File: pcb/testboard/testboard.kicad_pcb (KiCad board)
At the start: 2 copper layers, 24 parts, among them IC1 TLE94112ESXUMA1, IC2 AP63203WU-7, J1 Left Socket, J2 Right Socket, J3 Motor 1, J4 Motor 2, J5 Motor 3, J6 USB_C_Receptacle_USB2.0_14P, SW1 Control, U1 CYPD3177-24LQXQ

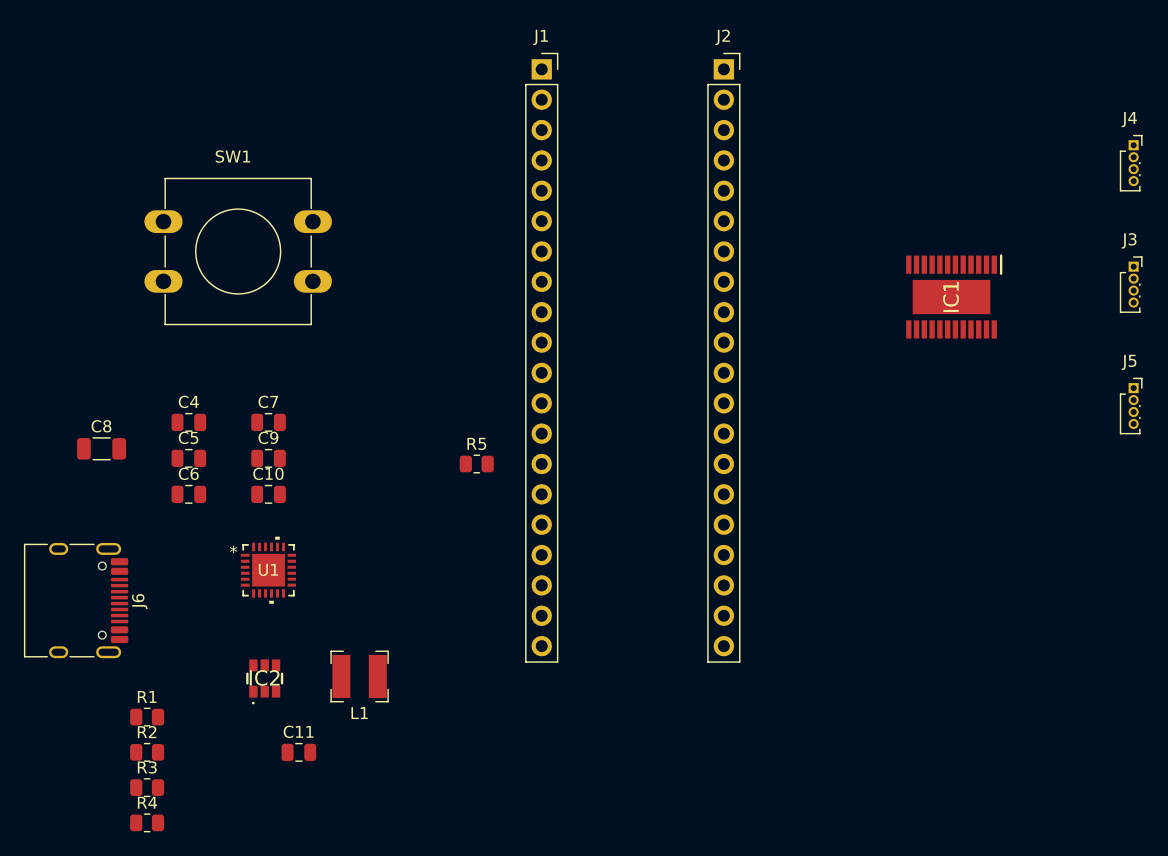
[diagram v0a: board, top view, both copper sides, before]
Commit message: initialized PCB design, added copper layer
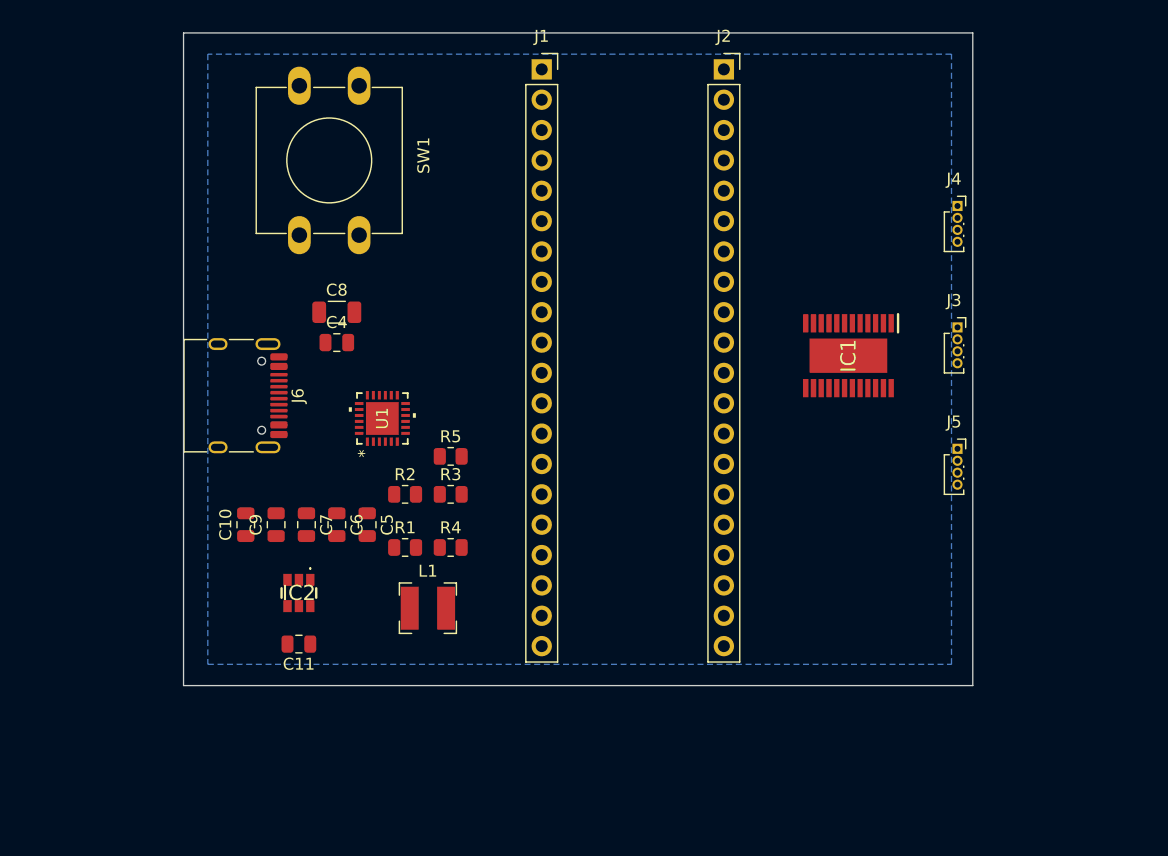
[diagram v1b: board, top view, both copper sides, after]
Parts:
- moved R3 35.3 mm to (82.5, 100.3)
- moved R4 34.3 mm to (82.5, 104.8)
- moved R2 30.5 mm to (78.7, 100.3)
- moved R1 25.8 mm to (78.7, 104.8)
- moved C8 22.8 mm to (73.0, 85.1)
- moved J6 21.7 mm to (64.1, 92.1)
- moved SW1 19.9 mm to (74.9, 66.1), turned to -90 degrees
- moved C5 15.9 mm to (75.6, 102.9), turned to -90 degrees
- moved U1 15.9 mm to (76.8, 94.0), turned to 90 degrees
- moved J3 15.6 mm to (125.0, 86.4)
- moved J4 15.6 mm to (125.0, 76.2)
- moved J5 15.6 mm to (125.0, 96.5)
- moved C4 14.1 mm to (73.0, 87.6)
- moved C6 12.6 mm to (73.0, 102.9), turned to -90 degrees
- moved IC1 9.92 mm to (115.8, 88.7)
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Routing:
- added copper zone on B.Cu, net GND
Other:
- board outline added: 66 x 54.6 mm

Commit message: PCB Routing added traces for left side of testboard
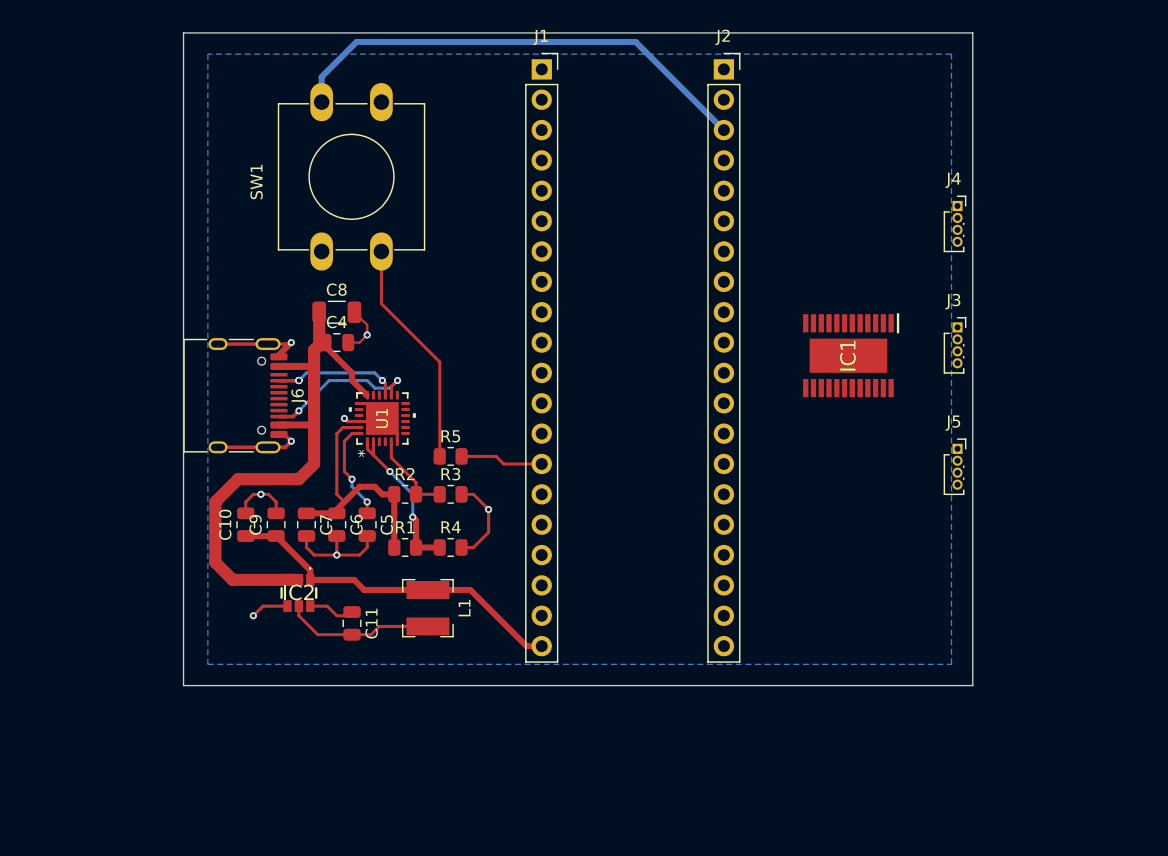
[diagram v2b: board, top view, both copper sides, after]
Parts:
- moved SW1 14.2 mm to (71.8, 80.0), turned to 90 degrees
- moved C11 4.77 mm to (74.3, 111.1), turned to -90 degrees
- turned L1 to 90 degrees
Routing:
- net /3V3: track 0.00 -> 69.1 mm
- net GND: track 0.00 -> 53.0 mm, vias 0 -> 8
- net /9V: track 0.00 -> 51.5 mm
- net /USB POWER/VDDD_REF: track 0.00 -> 21.0 mm
- net Net-(R5-Pad1): track 0.00 -> 19.2 mm
- net /USB POWER/VBUS_MAX: track 0.00 -> 13.6 mm, vias 0 -> 2
- net /USB POWER/CC2_SIG: track 0.00 -> 13.1 mm, vias 0 -> 2
- net Net-(IC2-SW): track 0.00 -> 12.5 mm
- net /USB POWER/CC1_SIG: track 0.00 -> 10.5 mm, vias 0 -> 4
- net Net-(U1B-VCCD): track 0.00 -> 8.33 mm, vias 0 -> 2
- net /USB POWER/ISNK_COARSE: track 0.00 -> 7.25 mm
- net /PB6: track 0.00 -> 6.97 mm
- net Net-(IC2-BST): track 0.00 -> 3.96 mm

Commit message: routed the new connectors
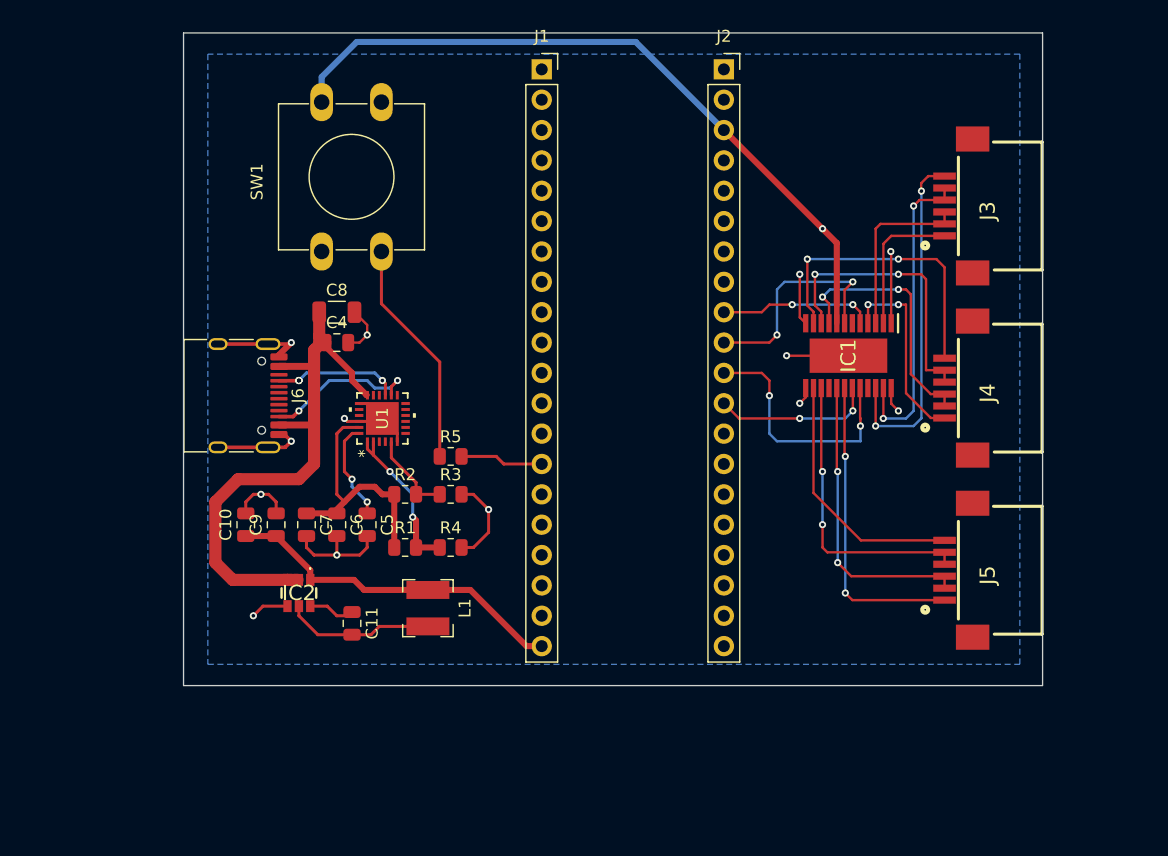
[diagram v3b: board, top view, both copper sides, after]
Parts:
- J3: value Motor 1 -> 52207-0633; footprint Connector_PinSocket_1.00mm:PinSocket_1x04_P1.00mm_Vertical -> molex:52207-0633
- J4: value Motor 2 -> 52207-0633; footprint Connector_PinSocket_1.00mm:PinSocket_1x04_P1.00mm_Vertical -> molex:52207-0633
- J5: value Motor 3 -> 52207-0633; footprint Connector_PinSocket_1.00mm:PinSocket_1x04_P1.00mm_Vertical -> molex:52207-0633
- moved J4 15.3 mm to (123.9, 91.4), turned to 90 degrees
- moved J5 10.2 mm to (123.9, 106.7), turned to 90 degrees
- moved J3 10.2 mm to (123.9, 76.2), turned to 90 degrees
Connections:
- J3 pad 3: /MOTOR DRIVER/OUT2 -> /MOTOR DRIVER/OUT5
- J3 pad 4: /MOTOR DRIVER/OUT8 -> /MOTOR DRIVER/OUT2
- J4 pad 3: /MOTOR DRIVER/OUT6 -> /MOTOR DRIVER/OUT9
- J4 pad 4: /MOTOR DRIVER/OUT4 -> /MOTOR DRIVER/OUT6
- J5 pad 3: /MOTOR DRIVER/OUT10 -> /MOTOR DRIVER/OUT11
- J5 pad 4: /MOTOR DRIVER/OUT3 -> /MOTOR DRIVER/OUT10
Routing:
- net /MOTOR DRIVER/OUT8: track 0.00 -> 29.2 mm, vias 0 -> 2
- net /MOTOR DRIVER/OUT2: track 0.00 -> 26.3 mm, vias 0 -> 2
- net /MOTOR DRIVER/OUT12: track 0.00 -> 25.7 mm, vias 0 -> 2
- net /MOTOR DRIVER/OUT11: track 0.00 -> 25.0 mm, vias 0 -> 2
- net /MOTOR DRIVER/OUT4: track 0.00 -> 25.0 mm, vias 0 -> 2
- net /MOTOR DRIVER/OUT10: track 0.00 -> 24.8 mm, vias 0 -> 2
- net /MOTOR DRIVER/OUT6: track 0.00 -> 24.0 mm, vias 0 -> 2
- net /MOTOR DRIVER/OUT9: track 0.00 -> 21.4 mm, vias 0 -> 2
- net /MOTOR DRIVER/OUT3: track 0.00 -> 21.4 mm
- net /PA5: track 0.00 -> 20.9 mm, vias 0 -> 2
- net /3V3: track 69.1 -> 89.3 mm, vias 0 -> 1
- net GND: track 53.0 -> 72.1 mm, vias 8 -> 13
- net /PA6: track 0.00 -> 18.9 mm, vias 0 -> 2
- net /MOTOR DRIVER/OUT7: track 0.00 -> 16.2 mm, vias 0 -> 2
- net /MOTOR DRIVER/OUT5: track 0.00 -> 14.8 mm
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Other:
- board size 66 x 54.6 mm -> 71.9 x 54.6 mm

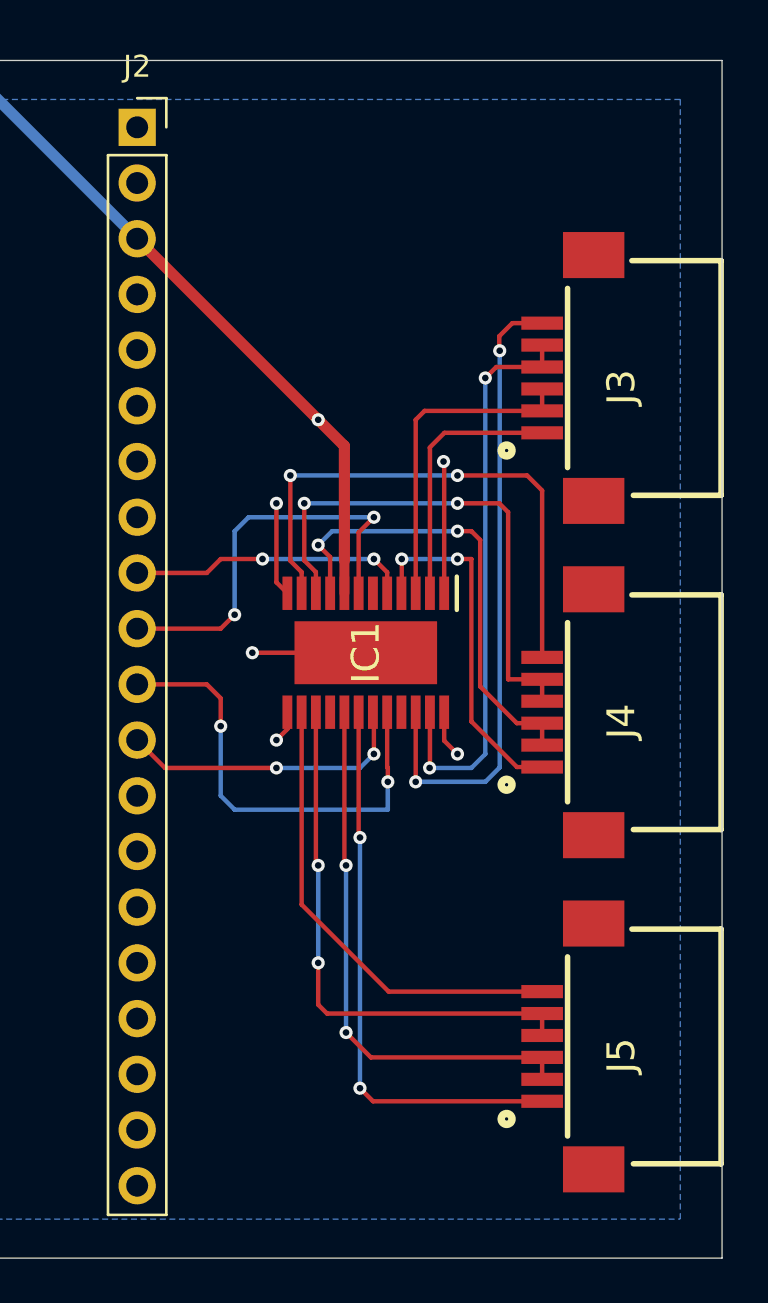
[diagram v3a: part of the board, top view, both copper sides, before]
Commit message: cleaned connectors routing
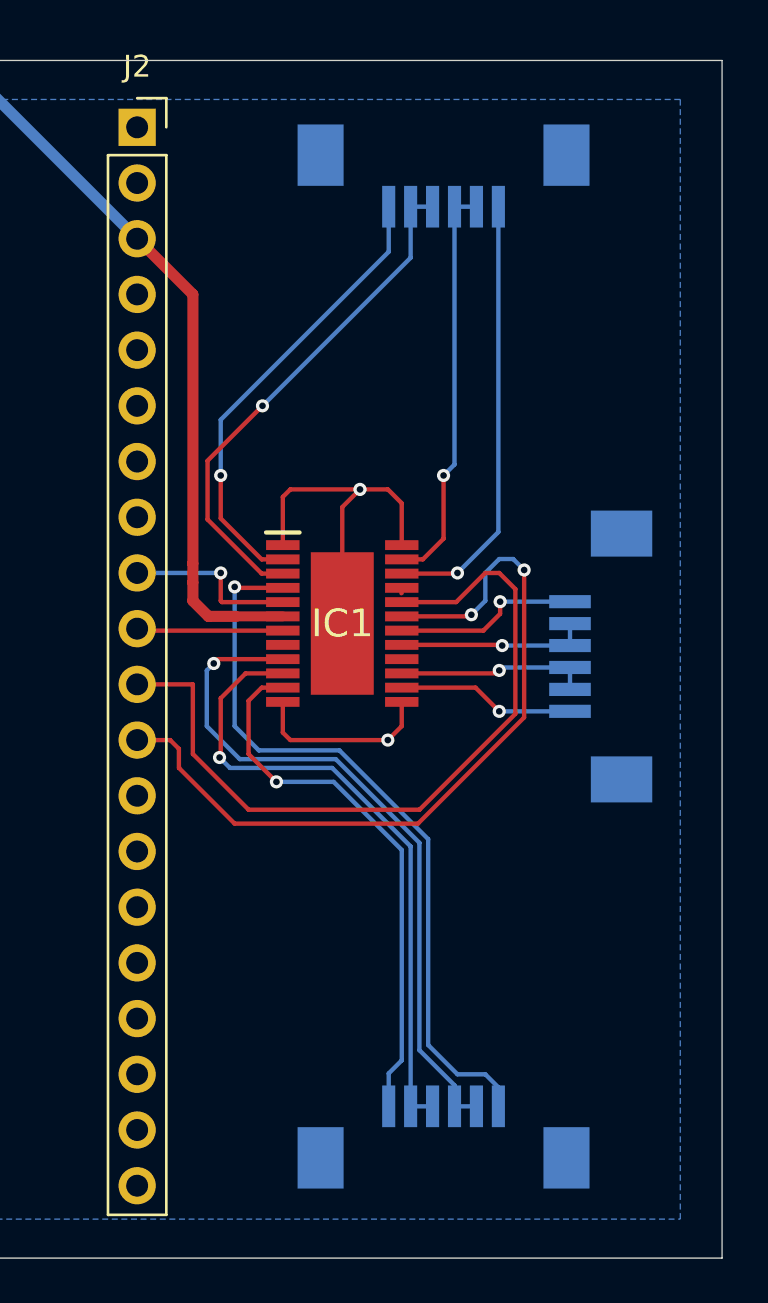
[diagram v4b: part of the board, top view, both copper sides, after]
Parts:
- J3, J4, J5: moved to B.Cu
- moved J4 18.5 mm to (119.4, 109.4), turned to 180 degrees
- moved J5 17.8 mm to (125.1, 88.9), turned to -90 degrees
- moved J3 9.01 mm to (119.4, 68.4), turned to 0 degrees
- moved IC1 1.71 mm to (114.8, 87.4), turned to 0 degrees
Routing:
- net /PA4: track 13.5 -> 36.1 mm
- net /MOTOR DRIVER/OUT7: track 16.2 -> 33.8 mm, vias 2 -> 1
- net /MOTOR DRIVER/OUT12: track 25.7 -> 8.54 mm, vias 2 -> 1
- net /MOTOR DRIVER/OUT11: track 25.0 -> 8.68 mm, vias 2 -> 1
- net /MOTOR DRIVER/OUT10: track 24.8 -> 8.78 mm, vias 2 -> 1
- net /PA5: track 20.9 -> 35.0 mm, vias 2 -> 0
- net /MOTOR DRIVER/OUT3: track 21.4 -> 8.12 mm, vias 0 -> 1
- net /PA6: track 18.9 -> 6.68 mm, vias 2 -> 0
- net /MOTOR DRIVER/OUT9: track 21.4 -> 31.8 mm, vias 2 -> 1
- net /MOTOR DRIVER/OUT8: track 29.2 -> 20.0 mm, vias 2 -> 1
- net /MOTOR DRIVER/OUT1: track 12.0 -> 21.0 mm, vias 0 -> 1
- net /MOTOR DRIVER/OUT5: track 14.8 -> 23.6 mm, vias 0 -> 1
- net /MOTOR DRIVER/OUT2: track 26.3 -> 18.6 mm, vias 2 -> 1
- net GND: track 72.1 -> 77.8 mm, vias 13 -> 10
- net /MOTOR DRIVER/OUT6: track 24.0 -> 29.3 mm, vias 2 -> 1
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
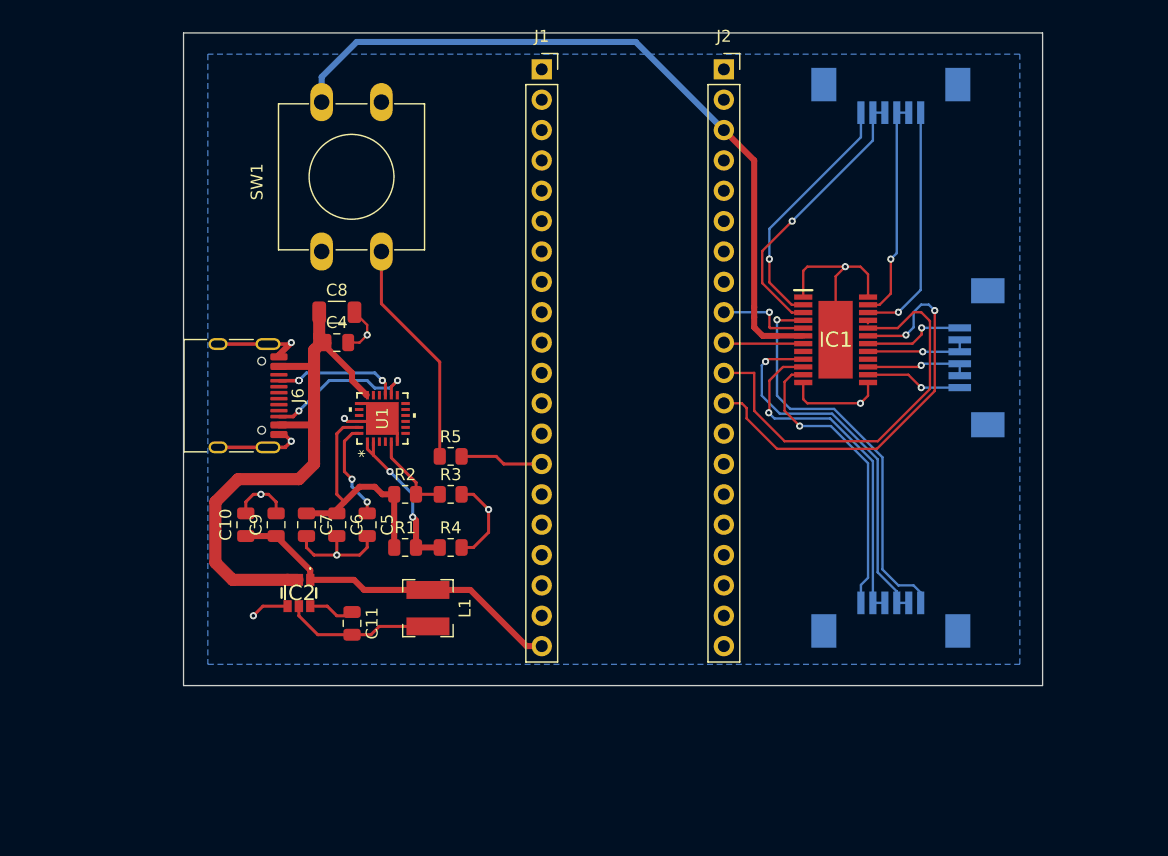
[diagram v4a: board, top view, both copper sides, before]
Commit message: Testboard PCB edits edited routing for motor & driver connections
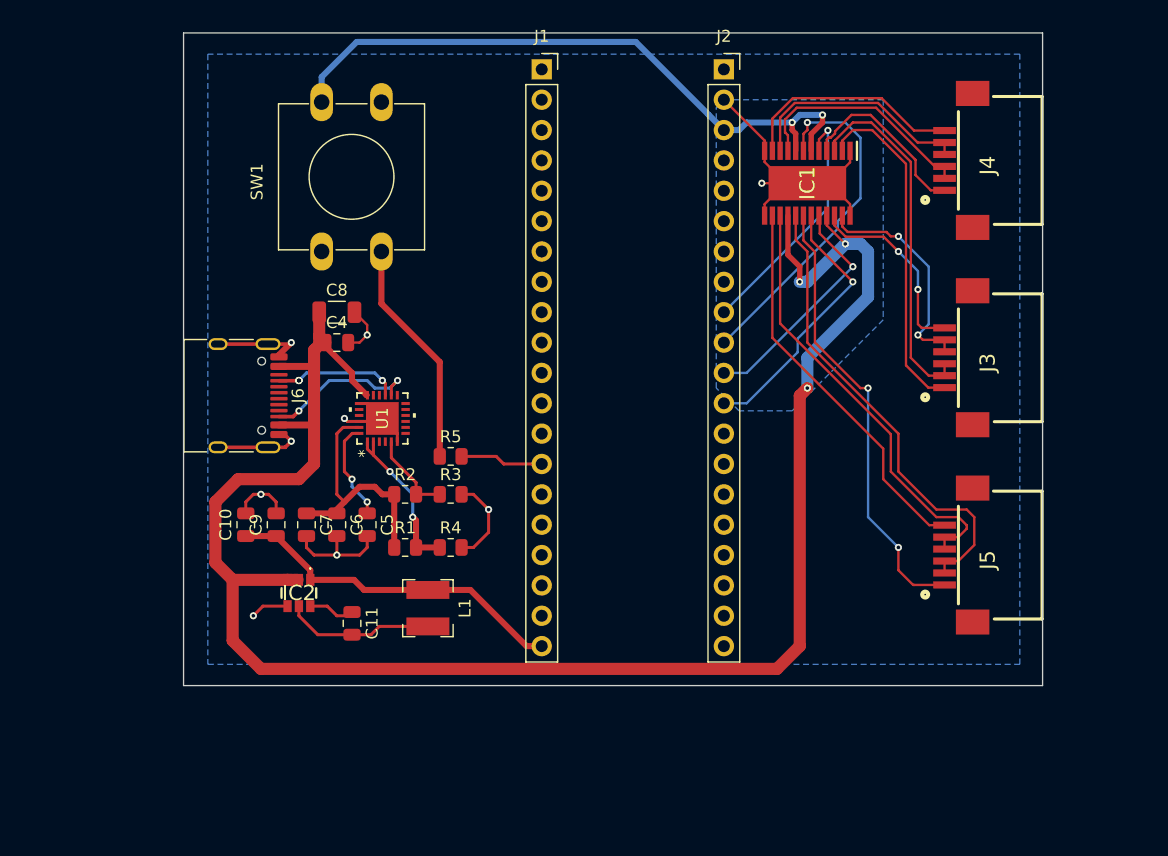
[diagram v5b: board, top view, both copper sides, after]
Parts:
- J3, J4, J5: moved to F.Cu
- moved J4 37.3 mm to (123.9, 72.4), turned to 90 degrees
- moved J3 21.0 mm to (123.9, 88.9), turned to 90 degrees
- moved J5 16.6 mm to (123.9, 105.4), turned to 90 degrees
- moved IC1 13.3 mm to (112.4, 74.3), turned to -90 degrees
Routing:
- net /9V: track 51.5 -> 157.4 mm, vias 0 -> 3
- net /MOTOR DRIVER/OUT11: track 8.68 -> 39.3 mm, vias 1 -> 0
- net /MOTOR DRIVER/OUT12: track 8.54 -> 37.7 mm, vias 1 -> 2
- net /MOTOR DRIVER/OUT10: track 8.78 -> 36.9 mm, vias 1 -> 0
- net /MOTOR DRIVER/OUT3: track 8.12 -> 32.6 mm, vias 1 -> 0
- net /PA6: track 6.68 -> 29.5 mm, vias 0 -> 1
- net /MOTOR DRIVER/OUT7: track 33.8 -> 15.1 mm, vias 1 -> 0
- net /PA5: track 35.0 -> 19.9 mm, vias 0 -> 1
- net /PA4: track 36.1 -> 22.7 mm, vias 2 -> 1
- net /PA7: track 7.94 -> 20.8 mm
- net /MOTOR DRIVER/OUT9: track 31.8 -> 19.5 mm, vias 1 -> 0
- net /MOTOR DRIVER/OUT6: track 29.3 -> 19.4 mm, vias 1 -> 0
- net /MOTOR DRIVER/OUT1: track 21.0 -> 28.6 mm, vias 1 -> 0
- net /3V3: track 91.0 -> 83.7 mm, vias 0 -> 2
- net /MOTOR DRIVER/OUT5: track 23.6 -> 30.1 mm, vias 1 -> 0
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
